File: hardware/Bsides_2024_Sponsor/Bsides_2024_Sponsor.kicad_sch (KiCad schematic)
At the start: 39 parts, among them J1 Conn_02x03_Odd_Even, J2 Battery, J3 Battery, J4 OLED, P1 USB_C_Plug_USB2.0, Q1 DMG3415U-7, SW1 ON, SW2 RESET, SW3 BOOT, SW4 RESET, SW6 RESET, U1 ESP32-C6-WROOM-1U-N4, U2 AP2112K-3.3

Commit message: feat(Hw):Update_Floorplan_Sponsor
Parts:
- removed J1: Conn_02x03_Odd_Even, Connector_PinSocket_2.54mm:PinSocket_2x03_P2.54mm_Vertical, symbol Connector_Generic:Conn_02x03_Odd_Even
- added C13: 1uF, Capacitor_SMD:C_0603_1608Metric, symbol Device:C_Small
- added C14, C15: 10uF, Capacitor_SMD:C_0603_1608Metric, symbol Device:C_Small
- added J5: Add_On, Connector_PinSocket_2.54mm:PinSocket_2x03_P2.54mm_Vertical, symbol Connector_Generic:Conn_02x03_Odd_Even
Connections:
- net +3V3: no longer C12.2, C2.1, C5.2, C6.2, C7.2, D2.1 (VDD), D3.1 (VDD), D4.1 (VDD), D5.1 (VDD), R1.2, R5.2, U1.2 (3V3), U2.5 (VOUT)
- net GND: now also C13.2, C14.2, C15.2, J5.2 (Pin_2)
- net SCL: now also J5.4 (Pin_4)
- net SDA: now also J5.3 (Pin_3)
- net VBUS: now also C1.1, U2.1 (VIN), U2.3 (EN); no longer D1.2 (A), Q1.1 (G), R2.1
- new net: C2.1, D1.2 (A), Q1.1 (G), R2.1, U2.5 (VOUT)
- new net VOUT: C12.2, C13.1, C14.1, C15.1, C5.2, C6.2, C7.2, D2.1 (VDD), D3.1 (VDD), D4.1 (VDD), D5.1 (VDD), J5.1 (Pin_1), R1.2, R5.2, SW1.2 (B), U1.2 (3V3)
- no-connect marks 13 -> 15
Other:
- moved on the sheet: C2, J2, J3, R1, U1

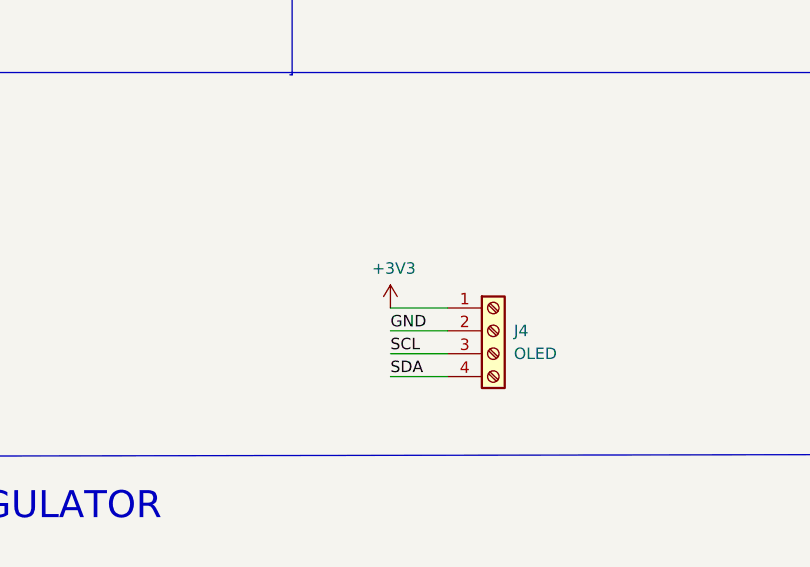
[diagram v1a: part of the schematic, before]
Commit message: feat(Hw):update_floorplan_sponsor
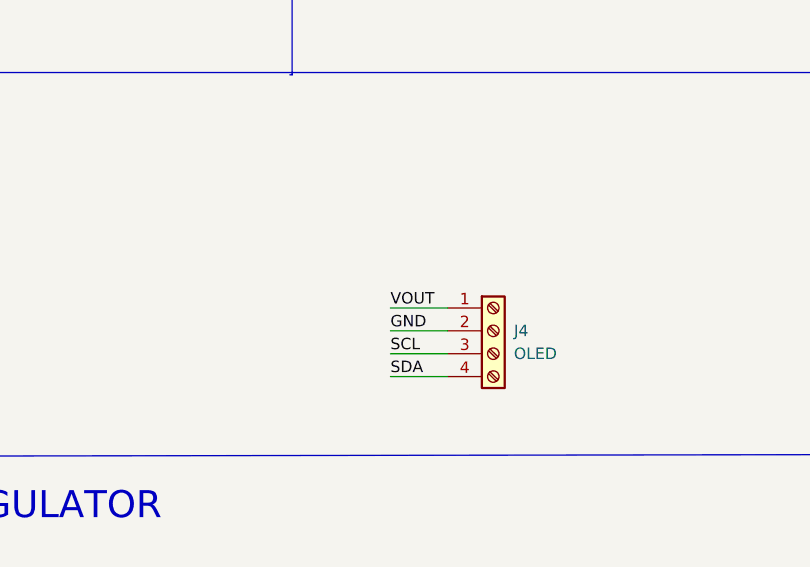
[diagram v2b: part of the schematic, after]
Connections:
- net +3V3 is gone; now on net VOUT: J4.1 (Pin_1)
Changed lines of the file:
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@@
 		)
 	)
+	(label "VOUT"
+		(at 96.266 124.206 0)
+		(fields_autoplaced yes)
+		(effects
+			(font
+				(size 1.27 1.27)
+			)
+			(justify left bottom)
+		)
+	)
 	(label "RX"
 		(at 74.676 63.246 0)
@@
 					(unit 1)
 				)
-			)
-		)
-	)
-	(symbol
-		(lib_id "power:+3V3")
-		(at 96.266 124.206 0)
-		(unit 1)
-		(exclude_from_sim no)
-		(in_bom yes)
-		(on_board yes)
-		(dnp no)
-		(property "Reference" "#PWR012"
-			(at 96.266 128.016 0)
-			(effects
-				(font
-					(size 1.27 1.27)
-				)
-				(hide yes)
-			)
-		)
-		(property "Value" "+3V3"
-			(at 96.647 119.8118 0)
-			(effects
-				(font
-					(size 1.27 1.27)
-				)
-			)
-		)
-		(property "Footprint" ""
-			(at 96.266 124.206 0)
-			(effects
-				(font
-					(size 1.27 1.27)
-				)
-				(hide yes)
-			)
-		)
-		(property "Datasheet" ""
-			(at 96.266 124.206 0)
-			(effects
-				(font
-					(size 1.27 1.27)
-				)
-				(hide yes)
-			)
-		)
-		(property "Description" ""
-			(at 96.266 124.206 0)
-			(effects
-				(font
-					(size 1.27 1.27)
-				)
-				(hide yes)
-			)
-		)
-		(pin "1"
-		)
-		(instances
-			(project "Bsides_2024_Sponsor"
-				(path "/ee1c7cbd-21da-443f-a57b-2be5d114455a"
-					(reference "#PWR012")
-					(unit 1)
-				)

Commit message: feat(Hw): Update schematics
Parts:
- removed J4: OLED, bsides:Display OLED 128 x32, symbol Connector:Screw_Terminal_01x04
- added J1: OLED, bsides:Display OLED 128 x32, symbol Connector:Screw_Terminal_01x04
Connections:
- net GND: now also J1.4 (Pin_4)
- net SCL: now also J1.2 (Pin_2)
- net SDA: now also J1.1 (Pin_1)
- net VOUT: now also J1.3 (Pin_3)
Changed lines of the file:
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@@
 	(wire
 		(pts
+			(xy 87.63 125.73) (xy 85.09 125.73)
+		)
+		(stroke
+			(width 0)
+			(type default)
+		)
+	)
+	(wire
+		(pts
 			(xy 172.974 187.579) (xy 173.99 187.579)
 		)
@@
 	(wire
 		(pts
+			(xy 87.63 123.19) (xy 85.09 123.19)
+		)
+		(stroke
+			(width 0)
+			(type default)
+		)
+	)
+	(wire
+		(pts
 			(xy 54.864 179.578) (xy 54.864 180.594)
 		)
@@
 	(wire
 		(pts
-			(xy 96.266 131.826) (xy 102.616 131.826)
+			(xy 225.806 129.794) (xy 234.95 129.794)
 		)
 		(stroke
@@
 	(wire
 		(pts
-			(xy 225.806 129.794) (xy 234.95 129.794)
+			(xy 70.866 74.422) (xy 74.676 74.422)
 		)
 		(stroke
@@
 	(wire
 		(pts
-			(xy 70.866 74.422) (xy 74.676 74.422)
+			(xy 129.032 45.72) (xy 131.572 45.72)
 		)
 		(stroke
@@
 	(wire
 		(pts
-			(xy 129.032 45.72) (xy 131.572 45.72)
+			(xy 87.63 118.11) (xy 85.09 118.11)
 		)
 		(stroke
@@
 	(wire
 		(pts
-			(xy 96.266 129.286) (xy 102.616 129.286)
+			(xy 79.248 179.324) (xy 79.248 181.102)
 		)
 		(stroke
@@
 	(wire
 		(pts
-			(xy 79.248 179.324) (xy 79.248 181.102)
+			(xy 77.216 172.466) (xy 79.248 172.466)
 		)
 		(stroke
@@
 	(wire
 		(pts
-			(xy 77.216 172.466) (xy 79.248 172.466)
+			(xy 87.63 120.65) (xy 85.09 120.65)
 		)
 		(stroke
@@
 	(wire
 		(pts
-			(xy 96.266 124.206) (xy 102.616 124.206)
-		)
-		(stroke
-			(width 0)
-			(type default)
-		)
-	)
-	(wire
-		(pts
 			(xy 122.174 38.1) (xy 125.222 38.1)
 		)
@@
 	(wire
 		(pts
-			(xy 96.266 126.746) (xy 102.616 126.746)
-		)
-		(stroke
-			(width 0)
-			(type default)
-		)
-	)
-	(wire
-		(pts
 			(xy 183.896 129.794) (xy 185.166 129.794)
 		)
@@
 		)
 	)
-	(label "GND"
-		(at 96.266 126.746 0)
-		(fields_autoplaced yes)
-		(effects
-			(font
-				(size 1.27 1.27)
-			)
-			(justify left bottom)
-		)
-	)
 	(label "PIN"
 		(at 173.228 129.794 0)
@@
 		)
 	)
+	(label "GND"
+		(at 85.09 125.73 180)
+		(fields_autoplaced yes)
+		(effects
+			(font
+				(size 1.27 1.27)
+			)
+			(justify right bottom)
+		)
+	)
 	(label "TX"
 		(at 74.676 60.452 0)
@@
 		)
 	)
+	(label "SCL"
+		(at 85.09 120.65 180)
+		(fields_autoplaced yes)
+		(effects
+			(font
+				(size 1.27 1.27)
+			)
+			(justify right bottom)
+		)
+	)
 	(label "BOOT"
 		(at 36.83 66.04 0)
@@
 		)
 	)
+	(label "SDA"
+		(at 85.09 118.11 180)
+		(fields_autoplaced yes)
+		(effects
+			(font
+				(size 1.27 1.27)
+			)
+			(justify right bottom)
+		)
+	)
 	(label "GPIO1"
 		(at 36.83 50.038 0)
@@
 		)
 	)
-	(label "D+"
-		(at 42.164 63.246 0)
-		(fields_autoplaced yes)
-		(effects
-			(font
-				(size 1.27 1.27)
-			)
-			(justify left bottom)
-		)
-	)
 	(label "VOUT"
-		(at 214.376 116.586 0)
+		(at 85.09 123.19 180)
 		(fields_autoplaced yes)
 		(effects
@@
 				(size 1.27 1.27)
 			)
-			(justify left bottom)
+			(justify right bottom)
 		)
 	)
-	(label "VOUT"
-		(at 32.004 75.438 0)
+	(label "D+"
+		(at 42.164 63.246 0)
 		(fields_autoplaced yes)
 		(effects
@@
 	)
 	(label "VOUT"
-		(at 27.94 112.014 0)
+		(at 214.376 116.586 0)
 		(fields_autoplaced yes)
 		(effects
@@
 		)
 	)
-	(label "SDA"
-		(at 96.266 131.826 0)
+	(label "VOUT"
+		(at 32.004 75.438 0)
 		(fields_autoplaced yes)
 		(effects
@@
 	)
 	(label "VOUT"
-		(at 96.266 124.206 0)
+		(at 27.94 112.014 0)
 		(fields_autoplaced yes)
 		(effects
@@
 		)
 	)
-	(label "SCL"
-		(at 96.266 129.286 0)
-		(fields_autoplaced yes)
-		(effects
-			(font
-				(size 1.27 1.27)
-			)
-			(justify left bottom)
-		)
-	)
 	(symbol
 		(lib_id "power:GND")
@@
 	)
 	(symbol
+		(lib_id "Connector:Screw_Terminal_01x04")
+		(at 92.71 120.65 0)
+		(unit 1)
+		(exclude_from_sim no)
+		(in_bom yes)
+		(on_board yes)
+		(dnp no)
+		(fields_autoplaced yes)
+		(property "Reference" "J1"
+			(at 94.996 120.6499 0)
+			(effects
+				(font
+					(size 1.27 1.27)
+				)
+				(justify left)
+			)
+		)
+		(property "Value" "OLED"
+			(at 94.996 123.1899 0)
+			(effects
+				(font
+					(size 1.27 1.27)
+				)
+				(justify left)
+			)
+		)
+		(property "Footprint" "bsides:Display OLED 128 x32"
+			(at 92.71 120.65 0)
+			(effects
+				(font
+					(size 1.27 1.27)
+				)
+				(hide yes)
+			)
+		)
+		(property "Datasheet" ""
+			(at 92.71 120.65 0)
+			(effects
+				(font
+					(size 1.27 1.27)
+				)
+				(hide yes)
+			)
+		)
+		(property "Description" ""
+			(at 92.71 120.65 0)
+			(effects
+				(font
+					(size 1.27 1.27)
+				)
+				(hide yes)
+			)
+		)
+		(property "manf#" "Display OLED 128×32 0.91 I2C SSD1306 Blanco / Azul"
+			(at 92.71 120.65 0)
+			(effects
+				(font
+					(size 1.27 1.27)
+				)
+				(hide yes)
+			)
+		)
+		(property "provedor" "UNIT Electronics"
+			(at 92.71 120.65 0)
+			(effects
+				(font
+					(size 1.27 1.27)
+				)
+				(hide yes)
+			)
+		)
+		(pin "1"
+		)
+		(pin "2"
+		)
+		(pin "3"
+		)
+		(pin "4"
+		)
+		(instances
+			(project "Bsides_2024_Sponsor"
+				(path "/ee1c7cbd-21da-443f-a57b-2be5d114455a"
+					(reference "J1")
+					(unit 1)
+				)
+			)
+		)
+	)
+	(symbol
 		(lib_id "Device:C_Small")
 		(at 258.191 87.122 270)
@@
 					(unit 1)
 				)
-			)
-		)
-	)
-	(symbol
-		(lib_id "Connector:Screw_Terminal_01x04")
-		(at 107.696 126.746 0)
-		(unit 1)
-		(exclude_from_sim no)
-		(in_bom yes)
-		(on_board yes)
-		(dnp no)
-		(fields_autoplaced yes)
-		(property "Reference" "J4"
-			(at 109.982 126.7459 0)
-			(effects
-				(font
-					(size 1.27 1.27)
-				)
-				(justify left)
-			)
-		)
-		(property "Value" "OLED"
-			(at 109.982 129.2859 0)
-			(effects
-				(font
-					(size 1.27 1.27)
-				)
-				(justify left)
-			)
-		)
-		(property "Footprint" "bsides:Display OLED 128 x32"
-			(at 107.696 126.746 0)
-			(effects
-				(font
-					(size 1.27 1.27)
-				)
-				(hide yes)
-			)
-		)
-		(property "Datasheet" "~"
-			(at 107.696 126.746 0)
-			(effects
-				(font
-					(size 1.27 1.27)
-				)
-				(hide yes)
-			)
-		)
-		(property "Description" ""
-			(at 107.696 126.746 0)
-			(effects
-				(font
-					(size 1.27 1.27)
-				)
-				(hide yes)
-			)
-		)
-		(property "manf#" "I2C SH1106 Display Oled Azul 128×64 1.3 ” "
-			(at 107.696 126.746 0)
-			(effects
-				(font
-					(size 1.27 1.27)
-				)
-				(hide yes)
-			)
-		)
-		(property "provedor" "UNIT Electronics"
-			(at 107.696 126.746 0)
-			(effects
-				(font
-					(size 1.27 1.27)
-				)
-				(hide yes)
-			)
-		)
-		(pin "1"
-		)
-		(pin "2"
-		)
-		(pin "3"
-		)
-		(pin "4"
-		)
-		(instances
-			(project "Bsides_2024_Sponsor"
-				(path "/ee1c7cbd-21da-443f-a57b-2be5d114455a"
-					(reference "J4")
-					(unit 1)
-				)

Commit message: feat(Hw):Update_Route_Sponsor
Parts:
- removed C10, C8, C9: 0.1uF, Capacitor_SMD:C_0603_1608Metric, symbol Device:C_Small
- removed C12, C5, C6, C7: 0.1uF, Capacitor_SMD:C_0603_1608Metric, symbol Device:C
- removed C15: 10uF, Capacitor_SMD:C_0603_1608Metric, symbol Device:C_Small
- removed J1: OLED, bsides:Display OLED 128 x32, symbol Connector:Screw_Terminal_01x04
- removed J2, J3: Battery, bsides:BH-AAA-A1aj001, symbol Connector:Screw_Terminal_01x02
- removed J5: Add_On, Connector_PinSocket_2.54mm:PinSocket_2x03_P2.54mm_Vertical, symbol Connector_Generic:Conn_02x03_Odd_Even
- added C10, C15, C8, C9: 0.1uF, Capacitor_SMD:C_0603_1608Metric, symbol Device:C
- added C12, C6, C7: 0.1uF, Capacitor_SMD:C_0603_1608Metric, symbol Device:C_Small
- added C5: 10uF, Capacitor_SMD:C_0603_1608Metric, symbol Device:C_Small
- added J1: Serial_IN, Connector_PinSocket_2.54mm:PinSocket_1x03_P2.54mm_Vertical, symbol Connector:Conn_01x03_Socket
- added J2: Add_On, Connector_PinSocket_2.54mm:PinSocket_2x03_P2.54mm_Vertical, symbol Connector_Generic:Conn_02x03_Odd_Even
- added J3: OLED, bsides:Display OLED 128 x32, symbol Connector:Screw_Terminal_01x04
- added J4: Serial_OUT, Connector_PinHeader_2.54mm:PinHeader_1x03_P2.54mm_Vertical, symbol Connector:Conn_01x03_Socket
- added J5, J6: Battery, bsides:BH-AA-A1AJ020, symbol Connector:Screw_Terminal_01x02
- C1: value 10uF -> 1uF; LCSC# C85713 -> C15849; Proveedor (none) -> Mouser; manf# (none) -> TMK107BJ105KA8T
- C11: LCSC# (none) -> C478888; Proveedor (none) -> Mouser; manf# (none) -> KAM15AR71C104KM
- C13: value 1uF -> 0.1uF; LCSC# C15849 -> C478888; Proveedor (none) -> Mouser; manf# (none) -> KAM15AR71C104KM; provedor LCSC -> (none)
- C14: value 10uF -> 0.1uF; LCSC# C85713 -> C478888; Proveedor (none) -> Mouser; manf# (none) -> KAM15AR71C104KM; provedor LCSC -> (none)
- C2: Proveedor (none) -> Mouser; manf# (none) -> GRM188R61E106KA73J
- C3, C4: value 0.1uF -> 10uF; LCSC# C478888 -> C85713; Proveedor (none) -> Mouser; manf# (none) -> GRM188R61E106KA73J
- D1: Proveedor (none) -> Mouser; manf# MBR120LSF -> MBR120LSFT1G
- D2, D3, D4, D5: manf# WS2812B-Mini -> (none)
- F1: LCSC# - -> (none); Proveedor (none) -> Mouser; manf# MFU0805FF00500P100 -> MFU0805FF00750P100
- P1: Proveedor (none) -> Mouser; manf# TYPE-C-31-M-31 -> USB4105-GF-A
- Q1: Proveedor (none) -> Mouser; manf# DMG3415U-7 -> DMG3415UQ-7
- R1: Proveedor (none) -> Mouser; manf# (none) -> ERJ-3GEYJ332V
- R2: Proveedor LCSC -> Mouser; manf# (none) -> RC0603DR-07100KL
- R3, R4: Proveedor (none) -> Mouser; manf# ERJ3RBD5101V -> AC0603DR-075K1L
- R5: Proveedor (none) -> Mouser; manf# CR-03JL7---10K -> RMC1/16K1002DTP
- R6: Proveedor (none) -> Mouser; manf# RTT03471JTP -> ERJ-3RBD4700V
- SW1, U2: Proveedor (none) -> Mouser
- SW2, SW3, SW5, SW7: Proveedor (none) -> Mouser; manf# (none) -> TL3342F160QG
- SW4, SW6: LCSC# C2886897 -> C318889; Proveedor (none) -> Mouser; manf# (none) -> TL3342F160QG
- U1: value ESP32-C6-WROOM-1U-N4 -> ESP32-C6-WROOM-1-N4; Proveedor (none) -> Mouser; manf# ESP32-C6-WROOM-1U-N4 -> ESP32-C6-WROOM-1-N4
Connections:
- net +BATT: now also J5.2 (Pin_2)
- net BOOT: now also C6.2; no longer C3.2
- net EN: now also C7.2; no longer C4.2
- net GND: now also C13.1, C14.1, C3.2, C4.2, C10.1, C12.1, C15.1, C5.2, C6.1, C7.1, C8.1, C9.1, J1.3 (Pin_3), J2.2 (Pin_2), J3.4 (Pin_4), J4.3 (Pin_3), J6.1 (Pin_1); no longer C13.2, C14.2, C3.1, C4.1
- net GPIO1: now also C11.2
- net GPIO15: now also SW5.2, C12.2; no longer SW6.2
- net GPIO22: now also C13.2, SW6.2; no longer SW5.2
- net GPIO23: now also C14.2; no longer C11.2
- net PIN: now also U1.11 (IO10); no longer R1.1, U1.10 (IO8)
- net SCL: now also J2.4 (Pin_4), J3.2 (Pin_2)
- net SDA: now also J2.3 (Pin_3), J3.1 (Pin_1)
- net VBUS: now also C4.1; no longer C1.1
- net VOUT: now also C1.1, C2.1, C3.1, SW1.3 (A), C10.2, C15.2, C8.2, C9.2, J2.1 (Pin_1), J3.3 (Pin_3); no longer C13.1, C14.1, SW1.2 (B)
- net GPIO3: now reaches U1.26 (IO3)
- net GPIO3: now also J2.5 (Pin_5)
- net GPIO2: now reaches U1.27 (IO2)
- net GPIO2: now also J2.6 (Pin_6)
- net GPIO4: now reaches U1.4 (IO4)
- net GPIO4: now also J4.1 (Pin_1)
- net GPIO5: now reaches U1.5 (IO5)
- net GPIO5: now also J4.2 (Pin_2)
- net at D1.2 (A), Q1.1 (G), R2.1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: now also C5.1; no longer C2.1
- net at D1.1 (K), Q1.2 (S): now also SW1.2 (B); no longer SW1.3 (A)
- net RX renamed GPIO17
- net GPIO17: now also J1.2 (Pin_2)
- net TX renamed GPIO16
- net GPIO16: now also J1.1 (Pin_1)
- new net: R1.1, U1.10 (IO8)
- new net: J5.1 (Pin_1), J6.2 (Pin_2)
- no-connect marks 15 -> 8
